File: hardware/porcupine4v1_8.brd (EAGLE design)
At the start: 24.4 x 27.4 mm, 32 parts, among them X1 PROGCON

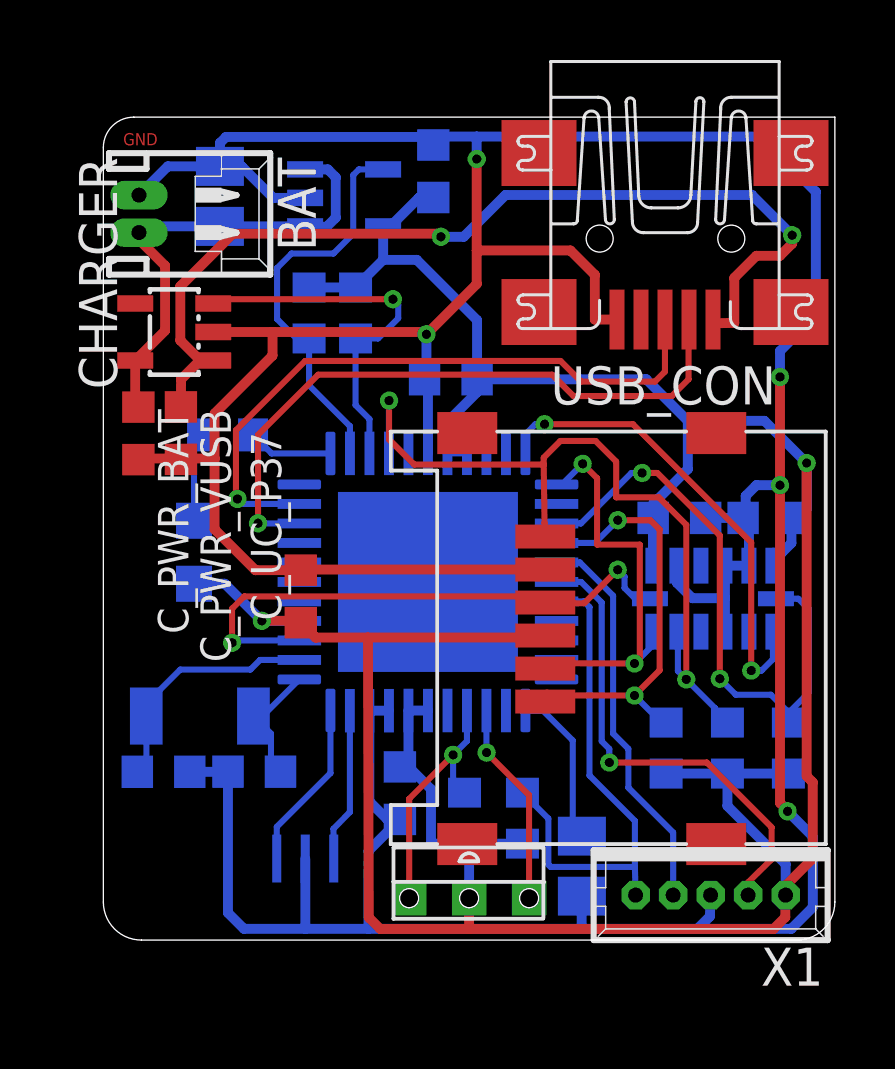
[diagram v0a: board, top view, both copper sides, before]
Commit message: porcupine4v1_8: added extension pins
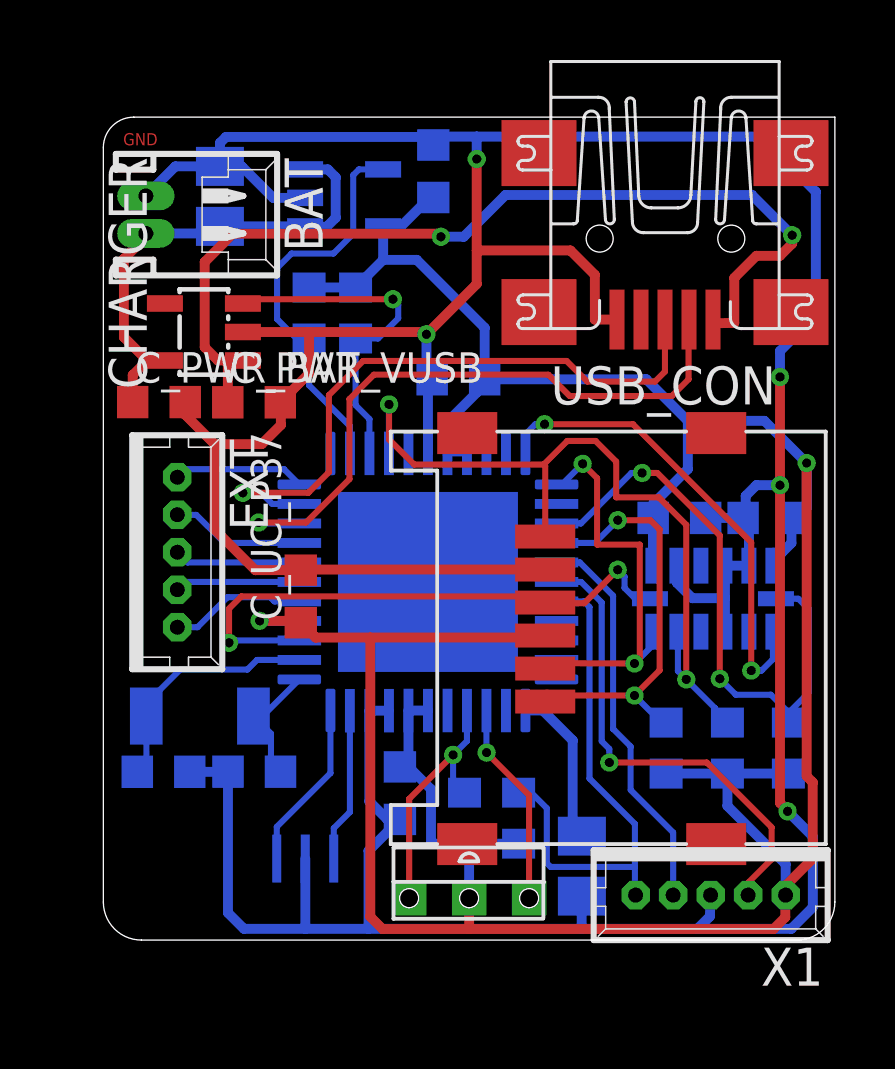
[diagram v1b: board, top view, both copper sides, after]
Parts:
- removed LED1: (no value), led:CHIPLED_0805
- removed R8: 10k, rcl:R0603
- added EXT: PROGCON, HedgehogLib:53047-05-OCT
- moved C_PWR_VUSB 2.65 mm to (5.02, 17.9), turned to 0 degrees
- moved C_PWR_BAT 1.25 mm to (1.85, 17.9), turned to 0 degrees
- moved CHARGER 0.99 mm to (3.35, 20.3)
- moved C_UC_P7/8 0.25 mm to (11.8, 18.7)
- moved BAT 0.23 mm to (2.67, 24.2)
- moved R1 0.13 mm to (13.8, 4.06)
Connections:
- removed net LED: PIC_CONTROLLER.1, R8.1
- removed net N$11: PIC_CONTROLLER.44
- new net EXT1: EXT.1, PIC_CONTROLLER.38
- new net EXT2: EXT.2, PIC_CONTROLLER.39
- new net EXT3: EXT.3, PIC_CONTROLLER.40
- new net EXT4: EXT.4, PIC_CONTROLLER.41
- new net EXT5: EXT.5, PIC_CONTROLLER.44
- net +3V3: no longer LED1.C
- net N$4: now also PIC_CONTROLLER.1; no longer LED1.A, R8.2
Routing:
- net EXT1: track 0.00 -> 4.54 mm
- net EXT4: track 0.00 -> 4.46 mm
- net EXT5: track 0.00 -> 4.39 mm
- net EXT3: track 0.00 -> 4.21 mm
- net EXT2: track 0.00 -> 4.18 mm
- net +3V3: track 113.1 -> 110.0 mm
- net N$4: track 2.97 -> 0.00 mm
- net LED: track 2.84 -> 0.00 mm
- net POK: track 12.5 -> 11.5 mm

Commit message: porcupine4v1_8: some wires rewired
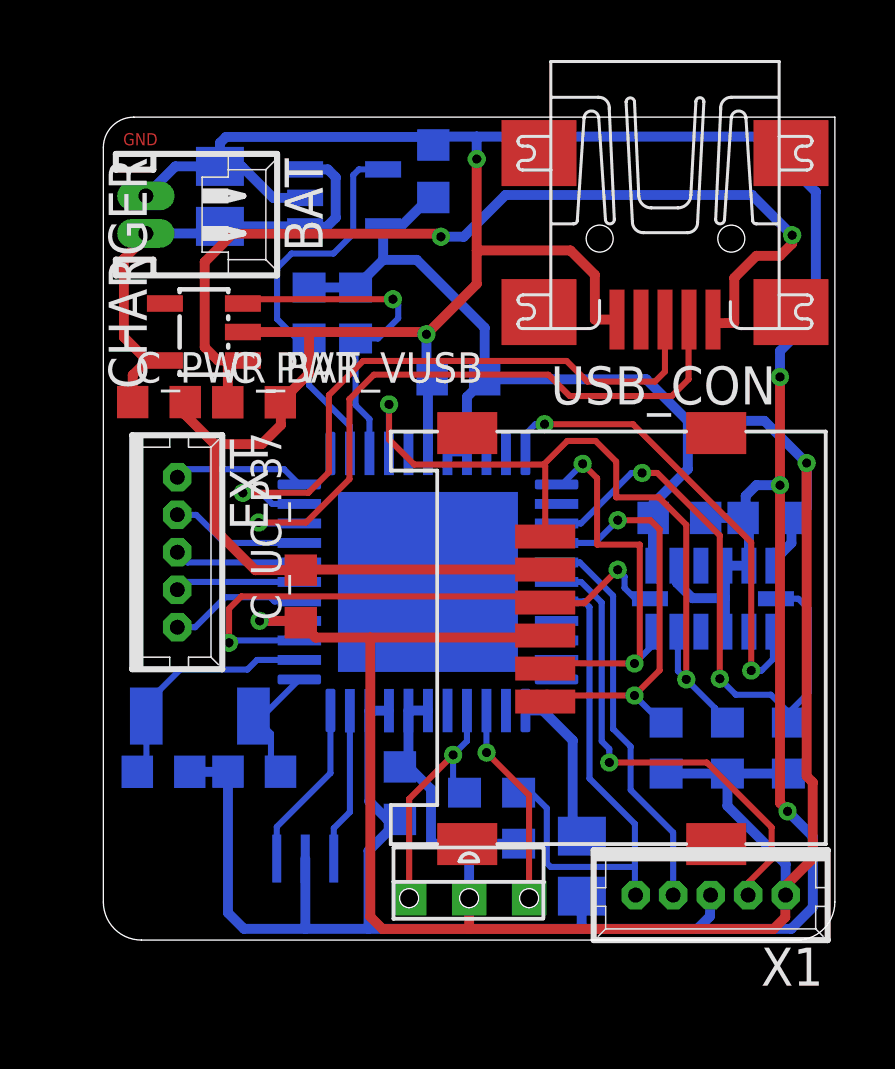
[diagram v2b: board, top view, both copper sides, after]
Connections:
- removed net N$4: PIC_CONTROLLER.1
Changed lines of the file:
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@@
 <wire x1="23.1" y1="14.0322" x2="23.0746" y2="14.0716" width="0.2032" layer="16"/>
 <wire x1="23.4442" y1="15.9004" x2="23.4442" y2="14.3764" width="0.3302" layer="16"/>
-<wire x1="11.4694" y1="17.272" x2="11.4694" y2="16.2235" width="0.3302" layer="16"/>
 <wire x1="12.192" y1="0.3702" x2="12.192" y2="1.397" width="0.3302" layer="1"/>
 <wire x1="12.192" y1="0.3702" x2="22.3412" y2="0.3702" width="0.3302" layer="1"/>
@@
 <wire x1="23.4442" y1="15.9004" x2="22.0358" y2="17.3088" width="0.3302" layer="16"/>
 <wire x1="22.0358" y1="17.3088" x2="19.4818" y2="17.3088" width="0.3302" layer="16"/>
-<wire x1="12.7114" y1="18.6944" x2="12.4574" y2="18.26" width="0.3302" layer="16"/>
-<wire x1="12.4574" y1="18.26" x2="11.4694" y2="17.272" width="0.3302" layer="16"/>
 <wire x1="18.0962" y1="18.6944" x2="12.7114" y2="18.6944" width="0.3302" layer="16"/>
 <wire x1="12.7114" y1="18.6944" x2="12.7114" y2="20.4102" width="0.3302" layer="16"/>
@@
 <wire x1="5.2116" y1="10.638" x2="5.207" y2="10.6426" width="0.3302" layer="16"/>
 <wire x1="6.5674" y1="10.6426" x2="5.207" y2="10.6426" width="0.3302" layer="1"/>
+<wire x1="12.7114" y1="18.6944" x2="12.1204" y2="18.1034" width="0.3302" layer="16"/>
+<wire x1="12.1204" y1="18.1034" x2="12.1204" y2="16.2255" width="0.3302" layer="16"/>
 </signal>
 <signal name="PROG_CLK@RB6">
@@
 <wire x1="6.5329" y1="11.288" x2="5.7046" y2="11.288" width="0.2032" layer="16"/>
 <wire x1="5.7046" y1="11.288" x2="5.5626" y2="11.43" width="0.2032" layer="16"/>
-<wire x1="5.5626" y1="11.43" x2="4.1402" y2="11.43" width="0.2032" layer="16"/>
-<wire x1="4.1402" y1="11.43" x2="3.1388" y2="10.4286" width="0.2032" layer="16"/>
-<wire x1="3.1388" y1="10.4286" x2="2.4638" y2="10.4286" width="0.2032" layer="16"/>
+<wire x1="5.5626" y1="11.43" x2="4.064" y2="11.43" width="0.2032" layer="16"/>
+<wire x1="4.064" y1="11.43" x2="3.0626" y2="10.4286" width="0.2032" layer="16"/>
+<wire x1="3.0626" y1="10.4286" x2="2.4638" y2="10.4286" width="0.2032" layer="16"/>
 </signal>
 <signal name="EXT2">
@@
 <wire x1="2.7324" y1="15.6972" x2="2.4638" y2="15.4286" width="0.2032" layer="16"/>
 </signal>
-<signal name="N$4">
-<contactref element="PIC_CONTROLLER" pad="1"/>
-</signal>
 </signals>

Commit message: 4.1.8 added bom & fixing
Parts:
- added LED1: (no value), led:SML0805
- added R8: 220, rcl:R0603
- moved C_UC_P28/29 0.84 mm to (9.96, 4.06)
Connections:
- new net N$4: LED1.A, R8.1
- net EXT4: no longer EXT.4
- net EXT5: now also EXT.4, R8.2; no longer EXT.5
- net GND: now also EXT.5, LED1.C
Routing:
- net GND: track 151.3 -> 158.0 mm
- net EXT4: track 4.46 -> 0.00 mm
- net EXT5: track 4.39 -> 7.95 mm
- net N$4: track 0.00 -> 2.57 mm
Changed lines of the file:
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@@
 <element name="C1_32KHZ" library="rcl" package="C0603K" value="22p" x="2.0066" y="5.6096" rot="MR180"/>
 <element name="C_UC_P7/8" library="rcl" package="C0603K" value="0.22u" x="11.8364" y="18.6944" rot="MR0"/>
-<element name="C_UC_P28/29" library="rcl" package="C0603K" value="0.22u" x="9.885" y="4.8968" rot="MR270"/>
+<element name="C_UC_P28/29" library="rcl" package="C0603K" value="0.22u" x="9.9612" y="4.064" rot="MR270"/>
 <element name="C_UC_P37" library="rcl" package="C0603K" value="0.1u" x="6.5814" y="11.4554" rot="R90"/>
 <element name="R1" library="rcl" package="R0603" value="10k" x="13.843" y="4.064" rot="MR270"/>
@@
 </element>
 <element name="EXT" library="HedgehogLib" package="53047-05-OCT" value="PROGCON" x="2.4638" y="12.9286" rot="R270"/>
+<element name="R8" library="rcl" package="R0603" value="220" x="4.5466" y="17.8816" rot="MR180"/>
+<element name="LED1" library="led" package="SML0805" value="" x="3.4798" y="19.5326" rot="MR180"/>
 </elements>
 <signals>
@@
 <wire x1="15.637" y1="1.4638" x2="15.5702" y2="1.397" width="0.3302" layer="16"/>
 <wire x1="15.9512" y1="1.4638" x2="15.637" y2="1.4638" width="0.3302" layer="16"/>
-<wire x1="6.731" y1="0.3756" x2="8.8392" y2="0.3756" width="0.3302" layer="16"/>
-<wire x1="8.8392" y1="0.3756" x2="15.9418" y2="0.3756" width="0.3302" layer="16"/>
+<wire x1="6.731" y1="0.3756" x2="8.8138" y2="0.3756" width="0.3302" layer="16"/>
+<wire x1="8.8138" y1="0.3756" x2="15.9418" y2="0.3756" width="0.3302" layer="16"/>
 <wire x1="21.4438" y1="13.8254" x2="21.52" y2="13.8254" width="0.2032" layer="16"/>
 <wire x1="21.3246" y1="14.0716" x2="21.4438" y2="13.8254" width="0.2032" layer="16"/>
@@
 <wire x1="10.9614" y1="18.6944" x2="10.7696" y2="18.8836" width="0.3302" layer="16"/>
 <wire x1="10.7696" y1="18.8836" x2="10.7696" y2="20.193" width="0.3302" layer="16"/>
-<wire x1="8.8392" y1="2.976" x2="8.8392" y2="0.3756" width="0.3302" layer="16"/>
 <wire x1="9.5204" y1="7.6465" x2="8.9596" y2="7.6445" width="0.3302" layer="16"/>
 <wire x1="8.9596" y1="7.6445" x2="8.8674" y2="7.6445" width="0.3302" layer="16"/>
@@
 <wire x1="4.6876" y1="0.3756" x2="4.1542" y2="0.909" width="0.3302" layer="16"/>
 <wire x1="4.1542" y1="0.909" x2="4.1542" y2="5.6134" width="0.3302" layer="16"/>
-<wire x1="9.885" y1="4.0218" x2="8.8392" y2="2.976" width="0.3302" layer="16"/>
-<wire x1="9.885" y1="4.0218" x2="9.4656" y2="4.0218" width="0.3302" layer="16"/>
-<wire x1="9.4656" y1="4.0218" x2="8.8674" y2="4.62" width="0.3302" layer="16"/>
-<wire x1="8.8674" y1="4.62" x2="8.8674" y2="7.6445" width="0.3302" layer="16"/>
+<wire x1="8.8674" y1="0.4292" x2="8.8674" y2="3.2258" width="0.3302" layer="16"/>
 <contactref element="LDO" pad="2"/>
 <contactref element="BAT" pad="2"/>
+<wire x1="8.8674" y1="3.2258" x2="8.8674" y2="7.6445" width="0.3302" layer="16"/>
 <wire x1="1.417" y1="24.8058" x2="2.4016" y2="25.7904" width="0.3302" layer="16"/>
 <wire x1="2.4016" y1="25.7904" x2="3.8862" y2="25.7904" width="0.3302" layer="16"/>
@@
 <wire x1="5.8982" y1="17.927" x2="6.858" y2="18.8868" width="0.3302" layer="1"/>
 <wire x1="6.858" y1="18.8868" x2="6.858" y2="20.2692" width="0.3302" layer="1"/>
-<wire x1="3.7084" y1="13.6906" x2="3.7084" y2="16.5322" width="0.3302" layer="1"/>
+<wire x1="3.7084" y1="13.6906" x2="3.7084" y2="15.8496" width="0.3302" layer="1"/>
+<wire x1="3.7084" y1="15.8496" x2="3.7084" y2="16.5322" width="0.3302" layer="1"/>
 <wire x1="2.7292" y1="17.9324" x2="2.7292" y2="17.5114" width="0.3302" layer="1"/>
 <wire x1="2.7292" y1="17.5114" x2="3.7084" y2="16.5322" width="0.3302" layer="1"/>
+<contactref element="LED1" pad="C"/>
+<contactref element="EXT" pad="5"/>
+<wire x1="2.4638" y1="15.4286" x2="3.2874" y2="15.4286" width="0.3302" layer="1"/>
+<wire x1="3.2874" y1="15.4286" x2="3.7084" y2="15.8496" width="0.3302" layer="1"/>
+<wire x1="2.4298" y1="19.5326" x2="1.9558" y2="19.5326" width="0.2032" layer="16"/>
+<wire x1="1.9558" y1="19.5326" x2="1.4478" y2="19.0246" width="0.2032" layer="16"/>
+<wire x1="1.4478" y1="19.0246" x2="1.4478" y2="16.4446" width="0.2032" layer="16"/>
+<wire x1="1.4478" y1="16.4446" x2="2.4638" y2="15.4286" width="0.2032" layer="16"/>
+<wire x1="8.8674" y1="0.4292" x2="8.8138" y2="0.3756" width="0.3302" layer="16"/>
+<wire x1="9.9612" y1="3.189" x2="8.9096" y2="3.1836" width="0.3302" layer="16"/>
+<wire x1="8.9096" y1="3.1836" x2="8.8674" y2="3.2258" width="0.3302" layer="16"/>
 </signal>
 <signal name="USB_D+@RC5">
@@
 <wire x1="10.8194" y1="7.6515" x2="10.1704" y2="7.6515" width="0.3302" layer="16"/>
 <wire x1="10.1704" y1="7.6515" x2="10.1704" y2="5.7524" width="0.3302" layer="16"/>
-<wire x1="10.1704" y1="5.7524" x2="9.885" y2="5.7718" width="0.3302" layer="16"/>
-<wire x1="12.0396" y1="3.214" x2="10.922" y2="3.214" width="0.3302" layer="16"/>
-<wire x1="10.922" y1="3.214" x2="10.922" y2="5.0292" width="0.3302" layer="16"/>
-<wire x1="10.922" y1="5.0292" x2="10.1794" y2="5.7718" width="0.3302" layer="16"/>
-<wire x1="10.1794" y1="5.7718" x2="9.885" y2="5.7718" width="0.3302" layer="16"/>
 <contactref element="LDO" pad="5"/>
 <wire x1="9.3265" y1="23.7896" x2="9.6786" y2="23.7896" width="0.3302" layer="16"/>
@@
 <wire x1="12.7114" y1="18.6944" x2="12.1204" y2="18.1034" width="0.3302" layer="16"/>
 <wire x1="12.1204" y1="18.1034" x2="12.1204" y2="16.2255" width="0.3302" layer="16"/>
+<wire x1="9.9612" y1="4.939" x2="9.9358" y2="5.5178" width="0.3302" layer="16"/>
+<wire x1="9.9358" y1="5.5178" x2="10.1704" y2="5.7524" width="0.3302" layer="16"/>
+<wire x1="10.0314" y1="5.0292" x2="9.9612" y2="4.939" width="0.3302" layer="16"/>
+<wire x1="12.0396" y1="3.214" x2="11.264" y2="3.214" width="0.3302" layer="16"/>
+<wire x1="11.264" y1="3.214" x2="11.049" y2="3.429" width="0.3302" layer="16"/>
+<wire x1="11.049" y1="3.429" x2="11.049" y2="4.7244" width="0.3302" layer="16"/>
+<wire x1="11.049" y1="4.7244" x2="10.8458" y2="4.9276" width="0.3302" layer="16"/>
+<wire x1="10.8458" y1="4.9276" x2="9.9418" y2="4.9276" width="0.3302" layer="16"/>
+<wire x1="9.9418" y1="4.9276" x2="9.9612" y2="4.939" width="0.3302" layer="16"/>
 </signal>
 <signal name="PROG_CLK@RB6">
@@
 </signal>
 <signal name="EXT4">
-<contactref element="EXT" pad="4"/>
 <contactref element="PIC_CONTROLLER" pad="41"/>
-<wire x1="6.5339" y1="13.238" x2="4.0394" y2="13.238" width="0.2032" layer="16"/>
-<wire x1="4.0394" y1="13.238" x2="3.0988" y2="14.1732" width="0.2032" layer="16"/>
-<wire x1="3.0988" y1="14.1732" x2="2.4638" y2="14.1786" width="0.2032" layer="16"/>
 </signal>
 <signal name="EXT5">
-<contactref element="EXT" pad="5"/>
 <contactref element="PIC_CONTROLLER" pad="44"/>
 <wire x1="6.5319" y1="15.188" x2="6.0227" y2="15.6972" width="0.2032" layer="16"/>
-<wire x1="6.0227" y1="15.6972" x2="2.7324" y2="15.6972" width="0.2032" layer="16"/>
-<wire x1="2.7324" y1="15.6972" x2="2.4638" y2="15.4286" width="0.2032" layer="16"/>
+<wire x1="6.0227" y1="15.6972" x2="4.9784" y2="15.6972" width="0.2032" layer="16"/>
+<contactref element="R8" pad="2"/>
+<wire x1="5.3966" y1="17.8816" x2="5.207" y2="17.8816" width="0.2032" layer="16"/>
+<wire x1="5.207" y1="17.8816" x2="5.207" y2="16.8148" width="0.2032" layer="16"/>
+<wire x1="5.207" y1="16.8148" x2="4.533" y2="16.1426" width="0.2032" layer="16"/>
+<wire x1="4.533" y1="16.1426" x2="4.9784" y2="15.6972" width="0.2032" layer="16"/>
+<contactref element="EXT" pad="4"/>
+<wire x1="2.4638" y1="14.1786" x2="3.3582" y2="14.1786" width="0.2032" layer="16"/>
+<wire x1="3.3582" y1="14.1786" x2="3.7338" y2="14.5542" width="0.2032" layer="16"/>
+<wire x1="3.7338" y1="14.5542" x2="3.7338" y2="15.3434" width="0.2032" layer="16"/>
+<wire x1="3.7338" y1="15.3434" x2="4.533" y2="16.1426" width="0.2032" layer="16"/>
+</signal>
+<signal name="N$4">
+<contactref element="LED1" pad="A"/>
+<contactref element="R8" pad="1"/>
+<wire x1="3.6966" y1="17.8816" x2="4.064" y2="17.9578" width="0.2032" layer="16"/>
+<wire x1="4.064" y1="17.9578" x2="4.064" y2="19.5326" width="0.2032" layer="16"/>
+<wire x1="4.064" y1="19.5326" x2="4.5298" y2="19.5326" width="0.2032" layer="16"/>
+<wire x1="4.6872" y1="19.5326" x2="4.5298" y2="19.5326" width="0.2032" layer="16"/>
 </signal>
 </signals>
